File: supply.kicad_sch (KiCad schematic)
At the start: 156 parts, among them J7 BarrelJack_3167288, J8 JST_SH_1x4_BM04B-SRSS-TB-LF-SN, Q12 SI7613DN-T1-GE3, Q13 SI7613DN-T1-GE3, Q14 BSS138PW, Q15 BSS138PW, Q16 BSS138PW, Q17 BSS138PW, SW4 SW_CVS-08TB, SW5 SW_KMR211NGLFS_SMD, U17 LTC4412IS6, U18 LTC4412IS6, U19 MPM54304GMN, U20 MPM54304GMN, U21 NCP718BSN330T1G, U22 MAX16150A_SOT, U25 PAC1954T-E_VQFN, U26 MAX812REUS+T, U27 MP8869S, U28 XC6230H001ER-G, U29 MCP4726A0T-E_MAY, U30 PAC1954T-E_VQFN, U31 LM3880

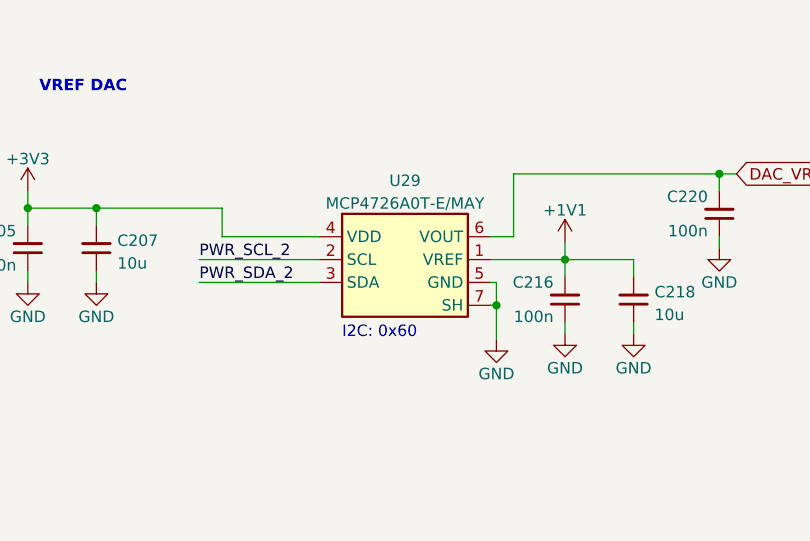
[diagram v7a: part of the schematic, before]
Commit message: Manually replace conflicted globlib files
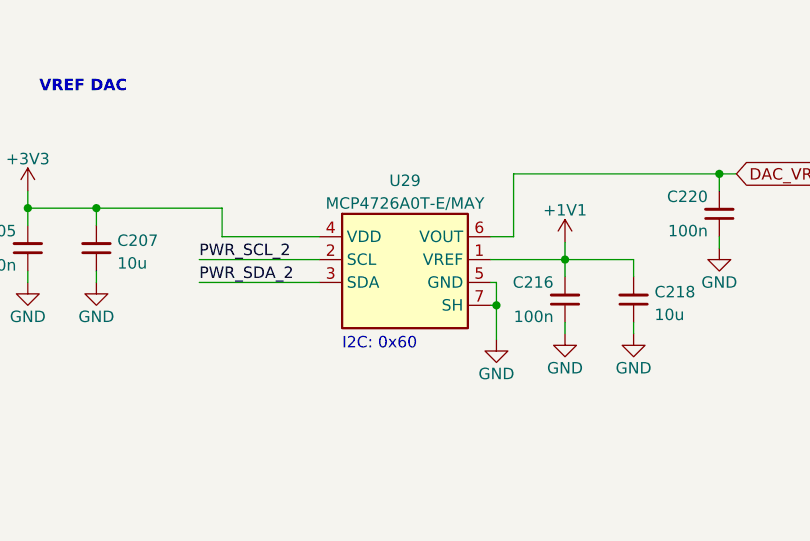
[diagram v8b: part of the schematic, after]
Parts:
- removed U29: MCP4726A0T-E_MAY, sodimm-ddr5-tester-footprints:DFN-6-1EP_2x2mm_P0.65mm_EP1x1.6mm, symbol sodimm-ddr5-tester:MCP4726A0T-E_MAY
- added U29: MCP4726A0T_DFN, antmicro-footprints:DFN-6-1EP_2x2mm_P0.65mm_EP1x1.6mm, symbol antmicroDataAcquisitionDigitaltoAnalogConvertersDAC:MCP4726A0T_DFN
- NT1, NT10, NT11, NT12, NT13, NT14, NT15, NT16, NT2, NT3, NT4, NT5, NT6, NT7, NT8, NT9: now left out of the parts list
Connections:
- net +1V1: now also U29.1 (VREF)
- net +3V3: now also U29.4 (VDD)
- net DAC_VREF: now also U29.6 (VOUT)
- net GND: now also U29.5 (GND), U29.7 (SH)
- net PWR_SCL_2: now also U29.2 (SCL)
- net PWR_SDA_2: now also U29.3 (SDA)
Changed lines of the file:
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@@
     (effects (font (size 1.27 1.27)) (justify left bottom))
   )
-  (text "I2C: 0x60" (at 342.265 328.295 0)
+  (text "I2C: 0x60" (at 342.265 329.565 0)
     (effects (font (size 1.27 1.27)) (justify left bottom))
   )
@@
     (pin "1")
   )
-  (symbol (lib_id "sodimm-ddr5-tester:MCP4726A0T-E_MAY") (at 339.725 316.865 0) (unit 1)
-    (in_bom yes) (on_board yes) (fields_autoplaced)
-    (property "Reference" "U29" (id 0) (at 349.25 310.64 0)
-      (effects (font (size 1.27 1.27) (thickness 0.15)))
-    )
-    (property "Value" "MCP4726A0T-E_MAY" (id 1) (at 372.745 327.025 0)
-      (effects (font (size 1.27 1.27) (thickness 0.15)) (justify left bottom) hide)
-    )
-    (property "Footprint" "sodimm-ddr5-tester-footprints:DFN-6-1EP_2x2mm_P0.65mm_EP1x1.6mm" (id 2) (at 372.745 329.565 0)
-      (effects (font (size 1.27 1.27) (thickness 0.15)) (justify left bottom) hide)
-    )
-    (property "Datasheet" "https://ww1.microchip.com/downloads/en/DeviceDoc/22272C.pdf" (id 3) (at 372.745 332.105 0)
-      (effects (font (size 1.27 1.27) (thickness 0.15)) (justify left bottom) hide)
-    )
-    (property "Manufacturer" "Microchip Technology" (id 4) (at 372.745 321.945 0)
-      (effects (font (size 1.27 1.27) (thickness 0.15)) (justify left bottom) hide)
-    )
-    (property "MPN" "MCP4726A0T-E/MAY" (id 5) (at 349.25 313.1637 0)
-      (effects (font (size 1.27 1.27) (thickness 0.15)))
-    )
-    (property "Author" "Antmicro" (id 6) (at 372.745 334.645 0)
-      (effects (font (size 1.27 1.27) (thickness 0.15)) (justify left bottom) hide)
-    )
-    (property "License" "Apache-2.0" (id 7) (at 372.745 337.185 0)
-      (effects (font (size 1.27 1.27) (thickness 0.15)) (justify left bottom) hide)
-    )
-    (pin "1")
-    (pin "2")
-    (pin "3")
-    (pin "4")
-    (pin "5")
-    (pin "6")
-    (pin "7")
-  )
   (symbol (lib_id "sodimm-ddr5-tester:GND") (at 34.29 66.675 0) (unit 1)
     (in_bom yes) (on_board yes) (fields_autoplaced)
@@
   )
   (symbol (lib_id "sodimm-ddr5-tester:Net-Tie_2") (at 113.03 224.155 90) (unit 1)
-    (in_bom yes) (on_board yes) (fields_autoplaced)
+    (in_bom no) (on_board yes) (fields_autoplaced)
     (property "Reference" "NT7" (id 0) (at 111.76 224.155 0)
       (effects (font (size 1.27 1.27)) hide)
@@
   )
   (symbol (lib_id "sodimm-ddr5-tester:Net-Tie_2") (at 113.03 162.56 90) (unit 1)
-    (in_bom yes) (on_board yes) (fields_autoplaced)
+    (in_bom no) (on_board yes) (fields_autoplaced)
     (property "Reference" "NT4" (id 0) (at 111.76 162.56 0)
       (effects (font (size 1.27 1.27)) hide)
@@
   )
   (symbol (lib_id "sodimm-ddr5-tester:Net-Tie_2") (at 121.285 184.785 90) (unit 1)
-    (in_bom yes) (on_board yes) (fields_autoplaced)
+    (in_bom no) (on_board yes) (fields_autoplaced)
     (property "Reference" "NT13" (id 0) (at 120.015 184.785 0)
       (effects (font (size 1.27 1.27)) hide)
@@
   )
   (symbol (lib_id "sodimm-ddr5-tester:Net-Tie_2") (at 113.03 104.14 90) (unit 1)
-    (in_bom yes) (on_board yes) (fields_autoplaced)
+    (in_bom no) (on_board yes) (fields_autoplaced)
     (property "Reference" "NT1" (id 0) (at 111.76 104.14 0)
       (effects (font (size 1.27 1.27)) hide)
@@
   )
   (symbol (lib_id "sodimm-ddr5-tester:Net-Tie_2") (at 113.665 239.395 90) (unit 1)
-    (in_bom yes) (on_board yes) (fields_autoplaced)
+    (in_bom no) (on_board yes) (fields_autoplaced)
     (property "Reference" "NT8" (id 0) (at 112.395 239.395 0)
       (effects (font (size 1.27 1.27)) hide)
@@
   )
   (symbol (lib_id "sodimm-ddr5-tester:Net-Tie_2") (at 121.285 104.14 90) (unit 1)
-    (in_bom yes) (on_board yes) (fields_autoplaced)
+    (in_bom no) (on_board yes) (fields_autoplaced)
     (property "Reference" "NT9" (id 0) (at 120.015 104.14 0)
       (effects (font (size 1.27 1.27)) hide)
@@
   )
   (symbol (lib_id "sodimm-ddr5-tester:Net-Tie_2") (at 121.92 239.395 90) (unit 1)
-    (in_bom yes) (on_board yes) (fields_autoplaced)
+    (in_bom no) (on_board yes) (fields_autoplaced)
     (property "Reference" "NT16" (id 0) (at 120.65 239.395 0)
       (effects (font (size 1.27 1.27)) hide)
@@
     (pin "1")
   )
+  (symbol (lib_id "antmicroDataAcquisitionDigitaltoAnalogConvertersDAC:MCP4726A0T_DFN") (at 339.725 316.865 0) (unit 1)
+    (in_bom yes) (on_board yes) (fields_autoplaced)
+    (property "Reference" "U29" (id 0) (at 349.25 310.64 0)
+      (effects (font (size 1.27 1.27) (thickness 0.15)))
+    )
+    (property "Value" "MCP4726A0T_DFN" (id 1) (at 372.745 324.485 0)
+      (effects (font (size 1.27 1.27) (thickness 0.15)) (justify left bottom) hide)
+    )
+    (property "Footprint" "antmicro-footprints:DFN-6-1EP_2x2mm_P0.65mm_EP1x1.6mm" (id 2) (at 372.745 327.025 0)
+      (effects (font (size 1.27 1.27) (thickness 0.15)) (justify left bottom) hide)
+    )
+    (property "Datasheet" "https://ww1.microchip.com/downloads/en/DeviceDoc/22272C.pdf" (id 3) (at 372.745 329.565 0)
+      (effects (font (size 1.27 1.27) (thickness 0.15)) (justify left bottom) hide)
+    )
+    (property "MPN" "MCP4726A0T-E/MAY" (id 4) (at 349.25 313.1637 0)
+      (effects (font (size 1.27 1.27) (thickness 0.15)))
+    )
+    (property "Manufacturer" "Microchip Technology" (id 5) (at 372.745 332.105 0)
+      (effects (font (size 1.27 1.27) (thickness 0.15)) (justify left bottom) hide)
+    )
+    (property "Author" "Antmicro" (id 6) (at 372.745 334.645 0)
+      (effects (font (size 1.27 1.27) (thickness 0.15)) (justify left bottom) hide)
+    )
+    (property "License" "Apache-2.0" (id 7) (at 372.745 337.185 0)
+      (effects (font (size 1.27 1.27) (thickness 0.15)) (justify left bottom) hide)
+    )
+    (pin "1")
+    (pin "2")
+    (pin "3")
+    (pin "4")
+    (pin "5")
+    (pin "6")
+    (pin "7")
+  )
   (symbol (lib_id "sodimm-ddr5-tester:C_10u_6.3V_0402") (at 314.96 320.675 90) (unit 1)
     (in_bom yes) (on_board yes) (fields_autoplaced)
@@
   )
   (symbol (lib_id "sodimm-ddr5-tester:Net-Tie_2") (at 113.03 143.51 90) (unit 1)
-    (in_bom yes) (on_board yes) (fields_autoplaced)
+    (in_bom no) (on_board yes) (fields_autoplaced)
     (property "Reference" "NT3" (id 0) (at 111.76 143.51 0)
       (effects (font (size 1.27 1.27)) hide)
@@
   )
   (symbol (lib_id "sodimm-ddr5-tester:Net-Tie_2") (at 113.03 206.375 90) (unit 1)
-    (in_bom yes) (on_board yes) (fields_autoplaced)
+    (in_bom no) (on_board yes) (fields_autoplaced)
     (property "Reference" "NT6" (id 0) (at 111.76 206.375 0)
       (effects (font (size 1.27 1.27)) hide)
@@
   )
   (symbol (lib_id "sodimm-ddr5-tester:Net-Tie_2") (at 121.285 143.51 90) (unit 1)
-    (in_bom yes) (on_board yes) (fields_autoplaced)
+    (in_bom no) (on_board yes) (fields_autoplaced)
     (property "Reference" "NT11" (id 0) (at 120.015 143.51 0)
       (effects (font (size 1.27 1.27)) hide)
@@
   )
   (symbol (lib_id "sodimm-ddr5-tester:Net-Tie_2") (at 121.285 125.73 90) (unit 1)
-    (in_bom yes) (on_board yes) (fields_autoplaced)
+    (in_bom no) (on_board yes) (fields_autoplaced)
     (property "Reference" "NT10" (id 0) (at 120.015 125.73 0)
       (effects (font (size 1.27 1.27)) hide)
@@
   )
   (symbol (lib_id "sodimm-ddr5-tester:Net-Tie_2") (at 121.285 224.155 90) (unit 1)
-    (in_bom yes) (on_board yes) (fields_autoplaced)
+    (in_bom no) (on_board yes) (fields_autoplaced)
     (property "Reference" "NT15" (id 0) (at 120.015 224.155 0)
       (effects (font (size 1.27 1.27)) hide)
@@
   )
   (symbol (lib_id "sodimm-ddr5-tester:Net-Tie_2") (at 113.03 125.73 90) (unit 1)
-    (in_bom yes) (on_board yes) (fields_autoplaced)
+    (in_bom no) (on_board yes) (fields_autoplaced)
     (property "Reference" "NT2" (id 0) (at 111.76 125.73 0)
       (effects (font (size 1.27 1.27)) hide)
@@
   )
   (symbol (lib_id "sodimm-ddr5-tester:Net-Tie_2") (at 113.03 184.785 90) (unit 1)
-    (in_bom yes) (on_board yes) (fields_autoplaced)
+    (in_bom no) (on_board yes) (fields_autoplaced)
     (property "Reference" "NT5" (id 0) (at 111.76 184.785 0)
       (effects (font (size 1.27 1.27)) hide)
@@
   )
   (symbol (lib_id "sodimm-ddr5-tester:Net-Tie_2") (at 121.285 206.375 90) (unit 1)
-    (in_bom yes) (on_board yes) (fields_autoplaced)
+    (in_bom no) (on_board yes) (fields_autoplaced)
     (property "Reference" "NT14" (id 0) (at 120.015 206.375 0)
       (effects (font (size 1.27 1.27)) hide)
@@
   )
   (symbol (lib_id "sodimm-ddr5-tester:Net-Tie_2") (at 121.285 162.56 90) (unit 1)
-    (in_bom yes) (on_board yes) (fields_autoplaced)
+    (in_bom no) (on_board yes) (fields_autoplaced)
     (property "Reference" "NT12" (id 0) (at 120.015 162.56 0)
       (effects (font (size 1.27 1.27)) hide)
